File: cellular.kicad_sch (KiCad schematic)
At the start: 48 parts, among them J2 SIM_Card, J4 SIM_Card, Q2 BC847, U10 SMF15CT1G, U11 SN74AXC4T245PWR, U5 SMF15CT1G

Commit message: lol
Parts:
- added ANT_GND1: SolderJumper_2_Open, Jumper:SolderJumper-2_P1.3mm_Open_Pad1.0x1.5mm, symbol Jumper:SolderJumper_2_Open
- added C47, C48: C, Capacitor_SMD:C_0603_1608Metric_Pad1.08x0.95mm_HandSolder, symbol Device:C
- added J8: CONMHF4-SMD-G-T, CONMHF4-SMD-G-T:TE_CONMHF4-SMD-G-T, symbol CONMHF4-SMD-G-T:CONMHF4-SMD-G-T
- added R39, R40: R, Resistor_SMD:R_0603_1608Metric_Pad0.98x0.95mm_HandSolder, symbol Device:R
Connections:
- net GND: now also ANT_GND1.1 (A), C47.1, C48.1
- net at U9.60 (RF_ANT): now also C48.2, R39.2
- new net: J8.1, R40.1
- new net: ANT_GND1.2 (B), J8.2, J8.3, J8.4
- new net: C47.2, R39.1, R40.2

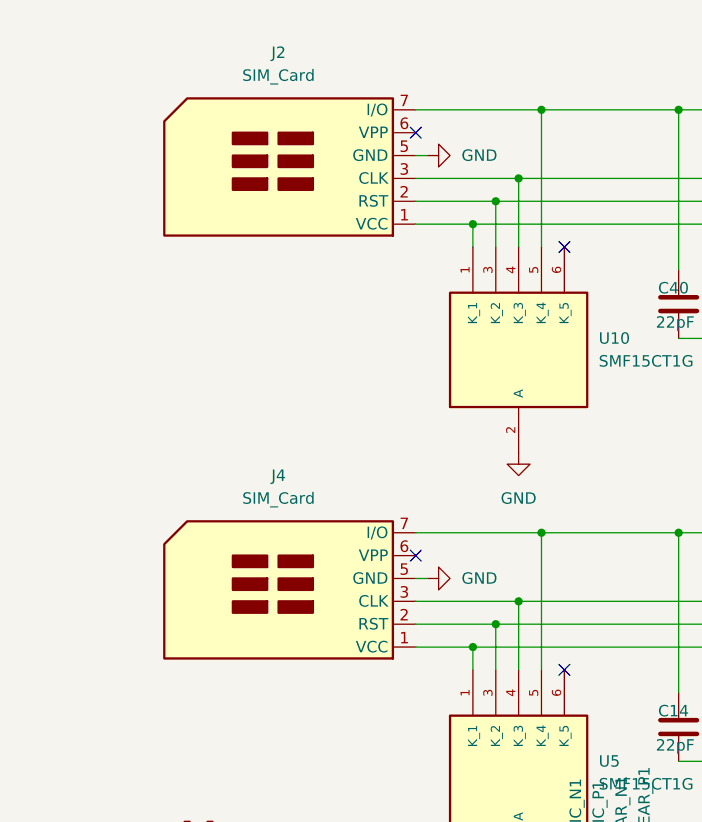
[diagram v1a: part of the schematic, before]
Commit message: what
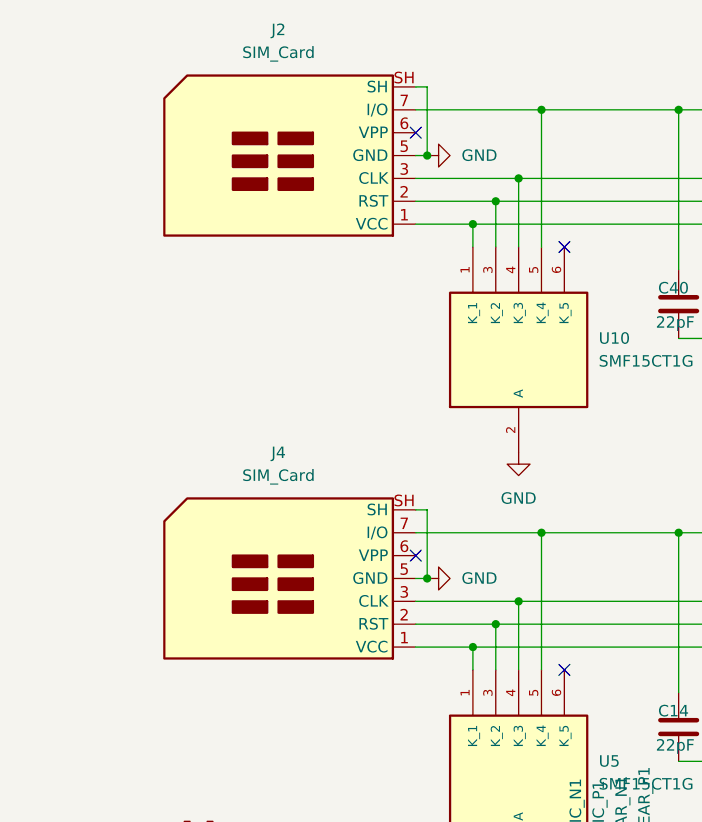
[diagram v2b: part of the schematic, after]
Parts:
- J2, J4: symbol Connector:SIM_Card -> Connector:SIM_Card_Shielded
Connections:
- net GND: now also J2.SH, J4.SH
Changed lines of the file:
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@@
 	)
 	(junction
+		(at 50.8 72.39)
+		(diameter 0)
+		(color 0 0 0 0)
+	)
+	(junction
 		(at 83.82 179.07)
 		(diameter 0)
@@
 	)
 	(junction
+		(at 50.8 25.4)
+		(diameter 0)
+		(color 0 0 0 0)
+	)
+	(junction
 		(at 48.26 179.07)
 		(diameter 0)
@@
 	(wire
 		(pts
+			(xy 50.8 17.78) (xy 50.8 25.4)
+		)
+		(stroke
+			(width 0)
+			(type default)
+		)
+	)
+	(wire
+		(pts
 			(xy 161.29 124.46) (xy 161.29 127)
 		)
@@
 	(wire
 		(pts
+			(xy 49.53 64.77) (xy 50.8 64.77)
+		)
+		(stroke
+			(width 0)
+			(type default)
+		)
+	)
+	(wire
+		(pts
 			(xy 74.93 109.22) (xy 74.93 127)
 		)
@@
 	(wire
 		(pts
+			(xy 49.53 17.78) (xy 50.8 17.78)
+		)
+		(stroke
+			(width 0)
+			(type default)
+		)
+	)
+	(wire
+		(pts
 			(xy 55.88 80.01) (xy 101.6 80.01)
 		)
@@
 	(wire
 		(pts
+			(xy 50.8 64.77) (xy 50.8 72.39)
+		)
+		(stroke
+			(width 0)
+			(type default)
+		)
+	)
+	(wire
+		(pts
 			(xy 101.6 38.1) (xy 97.79 38.1)
 		)
@@
 	)
 	(symbol
-		(lib_id "Connector:SIM_Card")
+		(lib_id "Connector:SIM_Card_Shielded")
 		(at 36.83 72.39 180)
 		(unit 1)
@@
 		(fields_autoplaced yes)
 		(property "Reference" "J4"
-			(at 34.29 60.96 0)
+			(at 34.29 58.42 0)
 			(effects
 				(font
@@
 		)
 		(property "Value" "SIM_Card"
-			(at 34.29 63.5 0)
+			(at 34.29 60.96 0)
 			(effects
 				(font
@@
 		(pin "7"
 		)
+		(pin "SH"
+		)
 		(instances
 			(project ""
@@
 	)
 	(symbol
-		(lib_id "Connector:SIM_Card")
+		(lib_id "Connector:SIM_Card_Shielded")
 		(at 36.83 25.4 180)
 		(unit 1)
@@
 		(fields_autoplaced yes)
 		(property "Reference" "J2"
-			(at 34.29 13.97 0)
+			(at 34.29 11.43 0)
 			(effects
 				(font
@@
 		)
 		(property "Value" "SIM_Card"
-			(at 34.29 16.51 0)
+			(at 34.29 13.97 0)
 			(effects
 				(font
@@
 		(pin "7"
 		)
+		(pin "SH"
+		)
 		(instances

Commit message: P
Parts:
- added PCM_CLK1, PCM_DI1, PCM_DO1, PCM_S1: TestPoint, TestPoint:TestPoint_Pad_D1.0mm, symbol Connector:TestPoint
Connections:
- net at U9.11 (PCM_CLK): now also PCM_CLK1.1
- net at U9.12 (PCM_SYNC): now also PCM_S1.1
- net at U9.13 (PCM_DIN): now also PCM_DI1.1
- net at U9.14 (PCM_DOUT): now also PCM_DO1.1
- no-connect marks 35 -> 31
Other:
- moved on the sheet: EAR_N1, EAR_P1, MIC_N1, MIC_P1
